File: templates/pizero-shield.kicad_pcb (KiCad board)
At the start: 2 copper layers, 65 x 30 mm, 5 parts

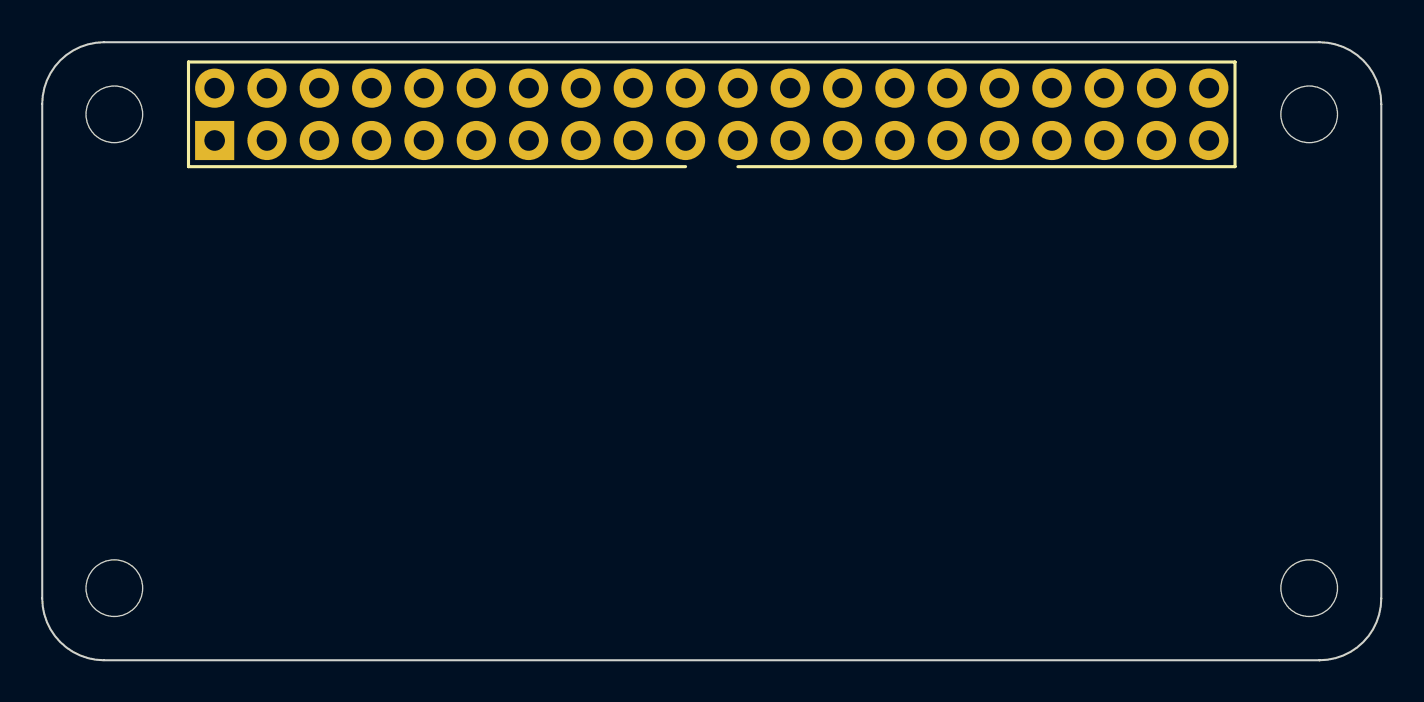
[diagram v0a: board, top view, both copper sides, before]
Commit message: Add M2.5_MOUNT and use it in the Pi templates
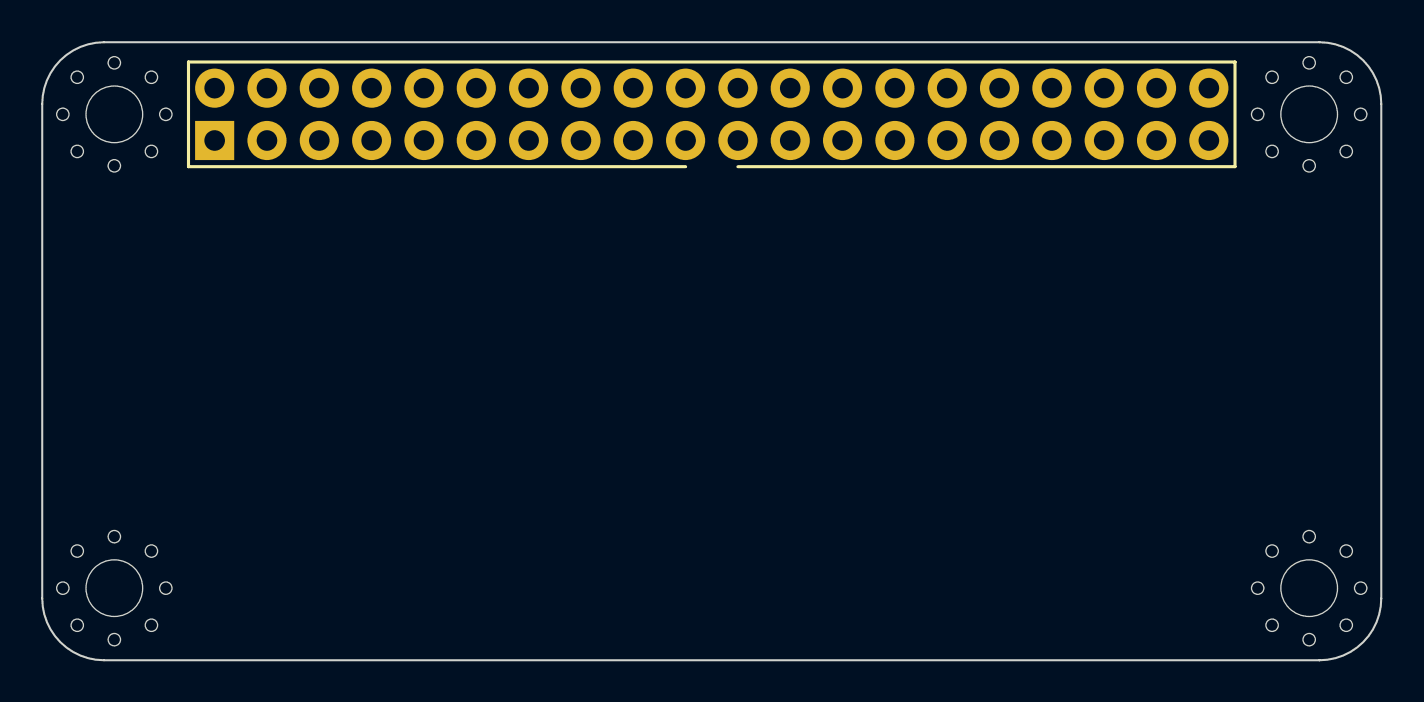
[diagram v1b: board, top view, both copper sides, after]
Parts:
- REF** (x4): value M3_HOLE -> M2.5_MOUNT; footprint agg:M2.5_HOLE -> agg:M2.5_MOUNT
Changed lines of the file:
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@@
     (links 0)
     (no_connects 0)
-    (area 111.891667 77.949999 177.108334 108.0925)
+    (area 110.558334 76.4425 178.441667 109.6925)
     (thickness 1.6)
     (drawings 8)
@@
     (uvia_drill 0.1)
   )
-  (module agg:M2.5_HOLE locked (layer F.Cu)
+  (module agg:M2.5_MOUNT locked (layer F.Cu)
     (at 115.5 104.5)
-    (solder_mask_margin 1.72)
-    (clearance 1.72)
-    (fp_text reference REF** (at 0 -2.5) (layer F.Fab) hide
+    (fp_text reference REF** (at 0 -4.1) (layer F.Fab) hide
       (effects (font (size 1 1) (thickness 0.15)))
     )
-    (fp_text value M3_HOLE (at 0 2.5) (layer F.Fab) hide
+    (fp_text value M2.5_MOUNT (at 0 4.1) (layer F.Fab) hide
       (effects (font (size 1 1) (thickness 0.15)))
     )
-    (fp_line (start -1.8 -1.8) (end 1.8 -1.8) (layer F.CrtYd) (width 0.01))
-    (fp_line (start 1.8 -1.8) (end 1.8 1.8) (layer F.CrtYd) (width 0.01))
-    (fp_line (start 1.8 1.8) (end -1.8 1.8) (layer F.CrtYd) (width 0.01))
-    (fp_line (start -1.8 1.8) (end -1.8 -1.8) (layer F.CrtYd) (width 0.01))
-    (pad "" np_thru_hole circle (at 0 0) (size 2.75 2.75) (drill 2.75) (layers *.Cu F.Mask))
+    (fp_line (start -3.4 -3.4) (end 3.4 -3.4) (layer F.CrtYd) (width 0.01))
+    (fp_line (start 3.4 -3.4) (end 3.4 3.4) (layer F.CrtYd) (width 0.01))
+    (fp_line (start 3.4 3.4) (end -3.4 3.4) (layer F.CrtYd) (width 0.01))
+    (fp_line (start -3.4 3.4) (end -3.4 -3.4) (layer F.CrtYd) (width 0.01))
+    (pad "" np_thru_hole circle (at 1.8 1.8) (size 0.6 0.6) (drill 0.6) (layers *.Cu *.Mask F.SilkS))
+    (pad "" np_thru_hole circle (at -1.8 1.8) (size 0.6 0.6) (drill 0.6) (layers *.Cu *.Mask F.SilkS))
+    (pad "" np_thru_hole circle (at 1.8 -1.8) (size 0.6 0.6) (drill 0.6) (layers *.Cu *.Mask F.SilkS))
+    (pad "" np_thru_hole circle (at -1.8 -1.8) (size 0.6 0.6) (drill 0.6) (layers *.Cu *.Mask F.SilkS))
+    (pad "" np_thru_hole circle (at -2.5 0) (size 0.6 0.6) (drill 0.6) (layers *.Cu *.Mask F.SilkS))
+    (pad "" np_thru_hole circle (at 0 2.5) (size 0.6 0.6) (drill 0.6) (layers *.Cu *.Mask F.SilkS))
+    (pad "" np_thru_hole circle (at 2.5 0) (size 0.6 0.6) (drill 0.6) (layers *.Cu *.Mask F.SilkS))
+    (pad "" np_thru_hole circle (at 0 -2.5) (size 0.6 0.6) (drill 0.6) (layers *.Cu *.Mask F.SilkS))
+    (pad "" np_thru_hole circle (at 0 0) (size 2.75 2.75) (drill 2.75) (layers *.Cu *.Mask F.SilkS)
+      (solder_mask_margin 1.72) (clearance 1.72))
   )
-  (module agg:M2.5_HOLE locked (layer F.Cu)
+  (module agg:M2.5_MOUNT locked (layer F.Cu)
     (at 173.5 104.5)
-    (solder_mask_margin 1.72)
-    (clearance 1.72)
-    (fp_text reference REF** (at 0 -2.5) (layer F.Fab) hide
+    (fp_text reference REF** (at 0 -4.1) (layer F.Fab) hide
       (effects (font (size 1 1) (thickness 0.15)))
     )
-    (fp_text value M3_HOLE (at 0 2.5) (layer F.Fab) hide
+    (fp_text value M2.5_MOUNT (at 0 4.1) (layer F.Fab) hide
       (effects (font (size 1 1) (thickness 0.15)))
     )
-    (fp_line (start -1.8 -1.8) (end 1.8 -1.8) (layer F.CrtYd) (width 0.01))
-    (fp_line (start 1.8 -1.8) (end 1.8 1.8) (layer F.CrtYd) (width 0.01))
-    (fp_line (start 1.8 1.8) (end -1.8 1.8) (layer F.CrtYd) (width 0.01))
-    (fp_line (start -1.8 1.8) (end -1.8 -1.8) (layer F.CrtYd) (width 0.01))
-    (pad "" np_thru_hole circle (at 0 0) (size 2.75 2.75) (drill 2.75) (layers *.Cu F.Mask))
+    (fp_line (start -3.4 -3.4) (end 3.4 -3.4) (layer F.CrtYd) (width 0.01))
+    (fp_line (start 3.4 -3.4) (end 3.4 3.4) (layer F.CrtYd) (width 0.01))
+    (fp_line (start 3.4 3.4) (end -3.4 3.4) (layer F.CrtYd) (width 0.01))
+    (fp_line (start -3.4 3.4) (end -3.4 -3.4) (layer F.CrtYd) (width 0.01))
+    (pad "" np_thru_hole circle (at 1.8 1.8) (size 0.6 0.6) (drill 0.6) (layers *.Cu *.Mask F.SilkS))
+    (pad "" np_thru_hole circle (at -1.8 1.8) (size 0.6 0.6) (drill 0.6) (layers *.Cu *.Mask F.SilkS))
+    (pad "" np_thru_hole circle (at 1.8 -1.8) (size 0.6 0.6) (drill 0.6) (layers *.Cu *.Mask F.SilkS))
+    (pad "" np_thru_hole circle (at -1.8 -1.8) (size 0.6 0.6) (drill 0.6) (layers *.Cu *.Mask F.SilkS))
+    (pad "" np_thru_hole circle (at -2.5 0) (size 0.6 0.6) (drill 0.6) (layers *.Cu *.Mask F.SilkS))
+    (pad "" np_thru_hole circle (at 0 2.5) (size 0.6 0.6) (drill 0.6) (layers *.Cu *.Mask F.SilkS))
+    (pad "" np_thru_hole circle (at 2.5 0) (size 0.6 0.6) (drill 0.6) (layers *.Cu *.Mask F.SilkS))
+    (pad "" np_thru_hole circle (at 0 -2.5) (size 0.6 0.6) (drill 0.6) (layers *.Cu *.Mask F.SilkS))
+    (pad "" np_thru_hole circle (at 0 0) (size 2.75 2.75) (drill 2.75) (layers *.Cu *.Mask F.SilkS)
+      (solder_mask_margin 1.72) (clearance 1.72))
   )
-  (module agg:M2.5_HOLE locked (layer F.Cu)
+  (module agg:M2.5_MOUNT locked (layer F.Cu)
     (at 173.5 81.5)
-    (solder_mask_margin 1.72)
-    (clearance 1.72)
-    (fp_text reference REF** (at 0 -2.5) (layer F.Fab) hide
+    (fp_text reference REF** (at 0 -4.1) (layer F.Fab) hide
       (effects (font (size 1 1) (thickness 0.15)))
     )
-    (fp_text value M3_HOLE (at 0 2.5) (layer F.Fab) hide
+    (fp_text value M2.5_MOUNT (at 0 4.1) (layer F.Fab) hide
       (effects (font (size 1 1) (thickness 0.15)))
     )
-    (fp_line (start -1.8 -1.8) (end 1.8 -1.8) (layer F.CrtYd) (width 0.01))
-    (fp_line (start 1.8 -1.8) (end 1.8 1.8) (layer F.CrtYd) (width 0.01))
-    (fp_line (start 1.8 1.8) (end -1.8 1.8) (layer F.CrtYd) (width 0.01))
-    (fp_line (start -1.8 1.8) (end -1.8 -1.8) (layer F.CrtYd) (width 0.01))
-    (pad "" np_thru_hole circle (at 0 0) (size 2.75 2.75) (drill 2.75) (layers *.Cu F.Mask))
+    (fp_line (start -3.4 -3.4) (end 3.4 -3.4) (layer F.CrtYd) (width 0.01))
+    (fp_line (start 3.4 -3.4) (end 3.4 3.4) (layer F.CrtYd) (width 0.01))
+    (fp_line (start 3.4 3.4) (end -3.4 3.4) (layer F.CrtYd) (width 0.01))
+    (fp_line (start -3.4 3.4) (end -3.4 -3.4) (layer F.CrtYd) (width 0.01))
+    (pad "" np_thru_hole circle (at 1.8 1.8) (size 0.6 0.6) (drill 0.6) (layers *.Cu *.Mask F.SilkS))
+    (pad "" np_thru_hole circle (at -1.8 1.8) (size 0.6 0.6) (drill 0.6) (layers *.Cu *.Mask F.SilkS))
+    (pad "" np_thru_hole circle (at 1.8 -1.8) (size 0.6 0.6) (drill 0.6) (layers *.Cu *.Mask F.SilkS))
+    (pad "" np_thru_hole circle (at -1.8 -1.8) (size 0.6 0.6) (drill 0.6) (layers *.Cu *.Mask F.SilkS))
+    (pad "" np_thru_hole circle (at -2.5 0) (size 0.6 0.6) (drill 0.6) (layers *.Cu *.Mask F.SilkS))
+    (pad "" np_thru_hole circle (at 0 2.5) (size 0.6 0.6) (drill 0.6) (layers *.Cu *.Mask F.SilkS))
+    (pad "" np_thru_hole circle (at 2.5 0) (size 0.6 0.6) (drill 0.6) (layers *.Cu *.Mask F.SilkS))
+    (pad "" np_thru_hole circle (at 0 -2.5) (size 0.6 0.6) (drill 0.6) (layers *.Cu *.Mask F.SilkS))
+    (pad "" np_thru_hole circle (at 0 0) (size 2.75 2.75) (drill 2.75) (layers *.Cu *.Mask F.SilkS)
+      (solder_mask_margin 1.72) (clearance 1.72))
   )
-  (module agg:M2.5_HOLE locked (layer F.Cu)
+  (module agg:M2.5_MOUNT locked (layer F.Cu)
     (at 115.5 81.5)
-    (solder_mask_margin 1.72)
-    (clearance 1.72)
-    (fp_text reference REF** (at 0 -2.5) (layer F.Fab) hide
+    (fp_text reference REF** (at 0 -4.1) (layer F.Fab) hide
       (effects (font (size 1 1) (thickness 0.15)))
     )
-    (fp_text value M3_HOLE (at 0 2.5) (layer F.Fab) hide
+    (fp_text value M2.5_MOUNT (at 0 4.1) (layer F.Fab) hide
       (effects (font (size 1 1) (thickness 0.15)))
     )
-    (fp_line (start -1.8 -1.8) (end 1.8 -1.8) (layer F.CrtYd) (width 0.01))
-    (fp_line (start 1.8 -1.8) (end 1.8 1.8) (layer F.CrtYd) (width 0.01))
-    (fp_line (start 1.8 1.8) (end -1.8 1.8) (layer F.CrtYd) (width 0.01))
-    (fp_line (start -1.8 1.8) (end -1.8 -1.8) (layer F.CrtYd) (width 0.01))
-    (pad "" np_thru_hole circle (at 0 0) (size 2.75 2.75) (drill 2.75) (layers *.Cu F.Mask))
+    (fp_line (start -3.4 -3.4) (end 3.4 -3.4) (layer F.CrtYd) (width 0.01))
+    (fp_line (start 3.4 -3.4) (end 3.4 3.4) (layer F.CrtYd) (width 0.01))
+    (fp_line (start 3.4 3.4) (end -3.4 3.4) (layer F.CrtYd) (width 0.01))
+    (fp_line (start -3.4 3.4) (end -3.4 -3.4) (layer F.CrtYd) (width 0.01))
+    (pad "" np_thru_hole circle (at 1.8 1.8) (size 0.6 0.6) (drill 0.6) (layers *.Cu *.Mask F.SilkS))
+    (pad "" np_thru_hole circle (at -1.8 1.8) (size 0.6 0.6) (drill 0.6) (layers *.Cu *.Mask F.SilkS))
+    (pad "" np_thru_hole circle (at 1.8 -1.8) (size 0.6 0.6) (drill 0.6) (layers *.Cu *.Mask F.SilkS))
+    (pad "" np_thru_hole circle (at -1.8 -1.8) (size 0.6 0.6) (drill 0.6) (layers *.Cu *.Mask F.SilkS))
+    (pad "" np_thru_hole circle (at -2.5 0) (size 0.6 0.6) (drill 0.6) (layers *.Cu *.Mask F.SilkS))
+    (pad "" np_thru_hole circle (at 0 2.5) (size 0.6 0.6) (drill 0.6) (layers *.Cu *.Mask F.SilkS))
+    (pad "" np_thru_hole circle (at 2.5 0) (size 0.6 0.6) (drill 0.6) (layers *.Cu *.Mask F.SilkS))
+    (pad "" np_thru_hole circle (at 0 -2.5) (size 0.6 0.6) (drill 0.6) (layers *.Cu *.Mask F.SilkS))
+    (pad "" np_thru_hole circle (at 0 0) (size 2.75 2.75) (drill 2.75) (layers *.Cu *.Mask F.SilkS)
+      (solder_mask_margin 1.72) (clearance 1.72))
   )
   (module agg:DIL-254P-40 locked (layer F.Cu)
